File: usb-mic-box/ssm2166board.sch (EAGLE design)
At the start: 10 parts, among them IC1 SSM2166S

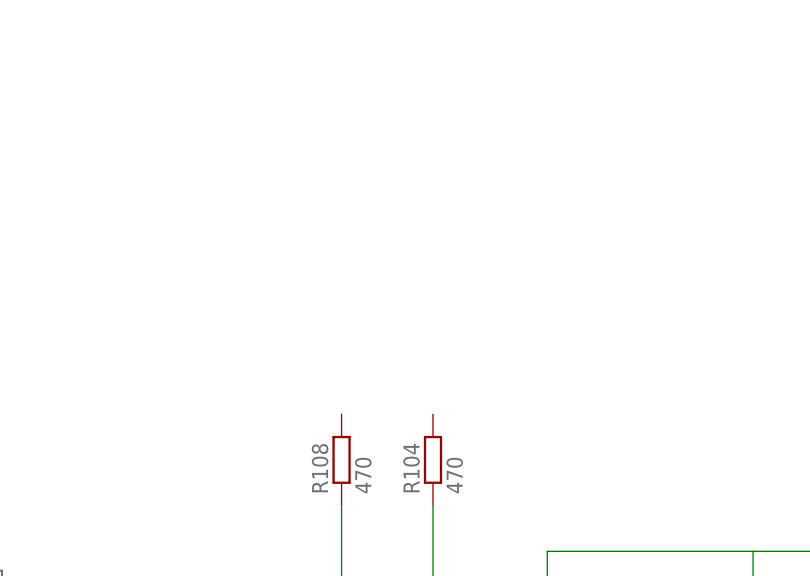
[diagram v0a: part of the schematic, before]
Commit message: Added my first library, and continuing SSM2166 schematics
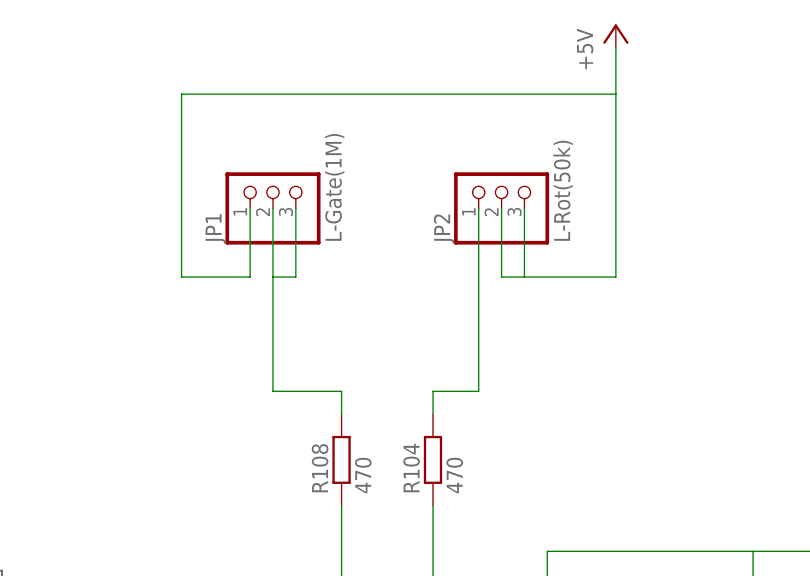
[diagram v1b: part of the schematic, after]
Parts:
- added JP1: L-Gate(1M), anton:PINHD-1X3
- added JP2: L-Rot(50k), anton:PINHD-1X3
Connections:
- new net N$8: JP1.2, JP1.3, R108.2
- new net N$9: JP2.1, R104.2
- net +5V: now also JP1.1, JP2.2, JP2.3
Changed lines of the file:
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@@
 <?xml version="1.0" encoding="utf-8"?>
 <!DOCTYPE eagle SYSTEM "eagle.dtd">
-<eagle version="6.2">
+<eagle version="6.3">
 <drawing>
 <settings>
@@
 <part name="C106" library="rcl" deviceset="CPOL-EU" device="E2-5" value="10uF"/>
 <part name="R181" library="rcl" deviceset="R-EU_" device="R1206" value="4.7k"/>
+<part name="JP1" library="anton" deviceset="PINHD-1X3" device="" value="L-Gate(1M)"/>
+<part name="JP2" library="anton" deviceset="PINHD-1X3" device="" value="L-Rot(50k)"/>
+<part name="P+2" library="supply1" deviceset="+5V" device=""/>
 </parts>
 <sheets>
@@
 <instance part="C106" gate="G$1" x="116.84" y="101.6" rot="R90"/>
 <instance part="R181" gate="G$1" x="139.7" y="111.76"/>
+<instance part="JP1" gate="A" x="73.66" y="152.4" rot="R90"/>
+<instance part="JP2" gate="A" x="99.06" y="152.4" rot="R90"/>
+<instance part="P+2" gate="1" x="111.76" y="170.18"/>
 </instances>
 <busses>
@@
 <pinref part="C103" gate="G$1" pin="1"/>
 <wire x1="15.24" y1="101.6" x2="15.24" y2="104.14" width="0.1524" layer="91"/>
+</segment>
+<segment>
+<pinref part="JP2" gate="A" pin="2"/>
+<wire x1="99.06" y1="149.86" x2="99.06" y2="142.24" width="0.1524" layer="91"/>
+<wire x1="99.06" y1="142.24" x2="101.6" y2="142.24" width="0.1524" layer="91"/>
+<pinref part="JP2" gate="A" pin="3"/>
+<wire x1="101.6" y1="149.86" x2="101.6" y2="142.24" width="0.1524" layer="91"/>
+<wire x1="101.6" y1="142.24" x2="111.76" y2="142.24" width="0.1524" layer="91"/>
+<wire x1="111.76" y1="142.24" x2="111.76" y2="162.56" width="0.1524" layer="91"/>
+<pinref part="P+2" gate="1" pin="+5V"/>
+<wire x1="111.76" y1="162.56" x2="111.76" y2="167.64" width="0.1524" layer="91"/>
+<wire x1="111.76" y1="162.56" x2="63.5" y2="162.56" width="0.1524" layer="91"/>
+<wire x1="63.5" y1="162.56" x2="63.5" y2="142.24" width="0.1524" layer="91"/>
+<wire x1="63.5" y1="142.24" x2="71.12" y2="142.24" width="0.1524" layer="91"/>
+<pinref part="JP1" gate="A" pin="1"/>
+<wire x1="71.12" y1="142.24" x2="71.12" y2="149.86" width="0.1524" layer="91"/>
 </segment>
 </net>
@@
 </segment>
 </net>
+<net name="N$8" class="0">
+<segment>
+<pinref part="R108" gate="G$1" pin="2"/>
+<wire x1="81.28" y1="127" x2="81.28" y2="129.54" width="0.1524" layer="91"/>
+<pinref part="JP1" gate="A" pin="2"/>
+<wire x1="81.28" y1="129.54" x2="73.66" y2="129.54" width="0.1524" layer="91"/>
+<wire x1="73.66" y1="129.54" x2="73.66" y2="142.24" width="0.1524" layer="91"/>
+<wire x1="73.66" y1="149.86" x2="73.66" y2="142.24" width="0.1524" layer="91"/>
+<pinref part="JP1" gate="A" pin="3"/>
+<wire x1="73.66" y1="142.24" x2="76.2" y2="142.24" width="0.1524" layer="91"/>
+<wire x1="76.2" y1="142.24" x2="76.2" y2="149.86" width="0.1524" layer="91"/>
+</segment>
+</net>
+<net name="N$9" class="0">
+<segment>
+<pinref part="R104" gate="G$1" pin="2"/>
+<wire x1="91.44" y1="127" x2="91.44" y2="129.54" width="0.1524" layer="91"/>
+<pinref part="JP2" gate="A" pin="1"/>
+<wire x1="91.44" y1="129.54" x2="96.52" y2="129.54" width="0.1524" layer="91"/>
+<wire x1="96.52" y1="129.54" x2="96.52" y2="149.86" width="0.1524" layer="91"/>
+</segment>
+</net>

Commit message: Continuing SSM2166 board schematics
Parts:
- added C101: 100nF, rcl:C-EUC1206
- added R1, R101: 10k, pot:TRIM_EU-CA6V
- added X1: PG203J, con-hirschmann:PG203J
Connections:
- new net N$10: IC1.-IN, R101.A
- new net N$11: R101.S, R181.2
- new net N$12: C101.1, R1.S, X1.5
- net +5V: now also R1.E
- net AGND: now also X1.1
- net N$3: now also C101.2
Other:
- moved on the sheet: C103
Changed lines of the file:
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@@
 <part name="JP2" library="anton" deviceset="PINHD-1X3" device="" value="L-Rot(50k)"/>
 <part name="P+2" library="supply1" deviceset="+5V" device=""/>
+<part name="R101" library="pot" deviceset="TRIM_EU-" device="CA6V" value="10k"/>
+<part name="C101" library="rcl" deviceset="C-EU" device="C1206" value="100nF"/>
+<part name="R1" library="pot" deviceset="TRIM_EU-" device="CA6V" value="10k"/>
+<part name="X1" library="con-hirschmann" deviceset="PG203J" device=""/>
 </parts>
 <sheets>
@@
 <instances>
 <instance part="IC1" gate="G$1" x="55.88" y="88.9"/>
-<instance part="P+1" gate="1" x="15.24" y="132.08"/>
-<instance part="C103" gate="G$1" x="15.24" y="99.06"/>
-<instance part="SUPPLY1" gate="G$1" x="15.24" y="40.64"/>
+<instance part="P+1" gate="1" x="10.16" y="139.7"/>
+<instance part="C103" gate="G$1" x="10.16" y="96.52"/>
+<instance part="SUPPLY1" gate="G$1" x="10.16" y="40.64"/>
 <instance part="C105" gate="G$1" x="99.06" y="55.88"/>
 <instance part="SUPPLY2" gate="G$1" x="99.06" y="40.64"/>
@@
 <instance part="JP2" gate="A" x="99.06" y="152.4" rot="R90"/>
 <instance part="P+2" gate="1" x="111.76" y="170.18"/>
+<instance part="R101" gate="1" x="152.4" y="111.76" rot="R180"/>
+<instance part="C101" gate="G$1" x="-7.62" y="96.52"/>
+<instance part="R1" gate="1" x="-7.62" y="109.22" rot="R270"/>
+<instance part="X1" gate="1" x="-48.26" y="58.42" rot="R180"/>
 </instances>
 <busses>
@@
 <segment>
 <pinref part="P+1" gate="1" pin="+5V"/>
-<wire x1="15.24" y1="129.54" x2="15.24" y2="104.14" width="0.1524" layer="91"/>
+<wire x1="10.16" y1="137.16" x2="10.16" y2="109.22" width="0.1524" layer="91"/>
 <pinref part="IC1" gate="G$1" pin="V+"/>
-<wire x1="15.24" y1="104.14" x2="38.1" y2="104.14" width="0.1524" layer="91"/>
 <pinref part="C103" gate="G$1" pin="1"/>
-<wire x1="15.24" y1="101.6" x2="15.24" y2="104.14" width="0.1524" layer="91"/>
+<wire x1="10.16" y1="109.22" x2="10.16" y2="104.14" width="0.1524" layer="91"/>
+<wire x1="10.16" y1="104.14" x2="38.1" y2="104.14" width="0.1524" layer="91"/>
+<wire x1="10.16" y1="99.06" x2="10.16" y2="104.14" width="0.1524" layer="91"/>
+<pinref part="R1" gate="1" pin="E"/>
+<wire x1="-2.54" y1="109.22" x2="10.16" y2="109.22" width="0.1524" layer="91"/>
+<junction x="10.16" y="109.22"/>
+<junction x="10.16" y="104.14"/>
 </segment>
 <segment>
@@
 <pinref part="JP1" gate="A" pin="1"/>
 <wire x1="71.12" y1="142.24" x2="71.12" y2="149.86" width="0.1524" layer="91"/>
+<junction x="101.6" y="142.24"/>
+<junction x="111.76" y="162.56"/>
 </segment>
 </net>
@@
 <pinref part="SUPPLY1" gate="G$1" pin="AGND"/>
 <pinref part="C103" gate="G$1" pin="2"/>
-<wire x1="15.24" y1="43.18" x2="15.24" y2="50.8" width="0.1524" layer="91"/>
+<wire x1="10.16" y1="43.18" x2="10.16" y2="50.8" width="0.1524" layer="91"/>
 <pinref part="C190" gate="G$1" pin="2"/>
-<wire x1="15.24" y1="50.8" x2="15.24" y2="93.98" width="0.1524" layer="91"/>
+<wire x1="10.16" y1="50.8" x2="10.16" y2="66.04" width="0.1524" layer="91"/>
+<wire x1="10.16" y1="66.04" x2="10.16" y2="91.44" width="0.1524" layer="91"/>
 <wire x1="22.86" y1="55.88" x2="22.86" y2="50.8" width="0.1524" layer="91"/>
-<wire x1="22.86" y1="50.8" x2="15.24" y2="50.8" width="0.1524" layer="91"/>
+<wire x1="22.86" y1="50.8" x2="10.16" y2="50.8" width="0.1524" layer="91"/>
 <pinref part="IC1" gate="G$1" pin="POWER_DOWN"/>
 <wire x1="38.1" y1="76.2" x2="33.02" y2="76.2" width="0.1524" layer="91"/>
@@
 <pinref part="IC1" gate="G$1" pin="GND"/>
 <wire x1="38.1" y1="73.66" x2="33.02" y2="73.66" width="0.1524" layer="91"/>
+<junction x="33.02" y="73.66"/>
+<junction x="22.86" y="50.8"/>
+<junction x="10.16" y="50.8"/>
+<pinref part="X1" gate="1" pin="1"/>
+<wire x1="-35.56" y1="66.04" x2="10.16" y2="66.04" width="0.1524" layer="91"/>
 </segment>
 <segment>
@@
 <wire x1="111.76" y1="50.8" x2="111.76" y2="48.26" width="0.1524" layer="91"/>
 <wire x1="111.76" y1="48.26" x2="99.06" y2="48.26" width="0.1524" layer="91"/>
+<junction x="99.06" y="48.26"/>
 </segment>
 </net>
@@
 <wire x1="99.06" y1="93.98" x2="129.54" y2="93.98" width="0.1524" layer="91"/>
 <wire x1="129.54" y1="93.98" x2="129.54" y2="78.74" width="0.1524" layer="91"/>
+<junction x="99.06" y="93.98"/>
 </segment>
 </net>
@@
 <wire x1="76.2" y1="96.52" x2="111.76" y2="96.52" width="0.1524" layer="91"/>
 <wire x1="111.76" y1="96.52" x2="111.76" y2="58.42" width="0.1524" layer="91"/>
-</segment>
-</net>
-<net name="N$3" class="0">
-<segment>
-<pinref part="C190" gate="G$1" pin="1"/>
-<wire x1="22.86" y1="63.5" x2="22.86" y2="86.36" width="0.1524" layer="91"/>
-<pinref part="IC1" gate="G$1" pin="+IN"/>
-<wire x1="22.86" y1="86.36" x2="38.1" y2="86.36" width="0.1524" layer="91"/>
 </segment>
 </net>
@@
 <pinref part="R181" gate="G$1" pin="1"/>
 <wire x1="134.62" y1="111.76" x2="127" y2="111.76" width="0.1524" layer="91"/>
+<junction x="127" y="111.76"/>
 </segment>
 </net>
@@
 <wire x1="73.66" y1="142.24" x2="76.2" y2="142.24" width="0.1524" layer="91"/>
 <wire x1="76.2" y1="142.24" x2="76.2" y2="149.86" width="0.1524" layer="91"/>
+<junction x="73.66" y="142.24"/>
 </segment>
 </net>
@@
 </segment>
 </net>
+<net name="N$10" class="0">
+<segment>
+<pinref part="IC1" gate="G$1" pin="-IN"/>
+<wire x1="38.1" y1="91.44" x2="33.02" y2="91.44" width="0.1524" layer="91"/>
+<wire x1="33.02" y1="91.44" x2="33.02" y2="132.08" width="0.1524" layer="91"/>
+<pinref part="R101" gate="1" pin="A"/>
+<wire x1="33.02" y1="132.08" x2="152.4" y2="132.08" width="0.1524" layer="91"/>
+<wire x1="152.4" y1="132.08" x2="152.4" y2="116.84" width="0.1524" layer="91"/>
+</segment>
+</net>
+<net name="N$11" class="0">
+<segment>
+<pinref part="R101" gate="1" pin="S"/>
+<pinref part="R181" gate="G$1" pin="2"/>
+<wire x1="147.32" y1="111.76" x2="144.78" y2="111.76" width="0.1524" layer="91"/>
+</segment>
+</net>
+<net name="N$3" class="0">
+<segment>
+<pinref part="IC1" gate="G$1" pin="+IN"/>
+<wire x1="22.86" y1="86.36" x2="38.1" y2="86.36" width="0.1524" layer="91"/>
+<pinref part="C190" gate="G$1" pin="1"/>
+<wire x1="22.86" y1="63.5" x2="22.86" y2="86.36" width="0.1524" layer="91"/>
+<wire x1="22.86" y1="86.36" x2="-7.62" y2="86.36" width="0.1524" layer="91"/>
+<pinref part="C101" gate="G$1" pin="2"/>
+<wire x1="-7.62" y1="86.36" x2="-7.62" y2="91.44" width="0.1524" layer="91"/>
+<junction x="22.86" y="86.36"/>
+</segment>
+</net>
+<net name="N$12" class="0">
+<segment>
+<pinref part="C101" gate="G$1" pin="1"/>
+<pinref part="R1" gate="1" pin="S"/>
+<wire x1="-7.62" y1="99.06" x2="-7.62" y2="101.6" width="0.1524" layer="91"/>
+<pinref part="X1" gate="1" pin="5"/>
+<wire x1="-7.62" y1="101.6" x2="-7.62" y2="104.14" width="0.1524" layer="91"/>
+<wire x1="-35.56" y1="55.88" x2="-15.24" y2="55.88" width="0.1524" layer="91"/>
+<wire x1="-15.24" y1="55.88" x2="-15.24" y2="101.6" width="0.1524" layer="91"/>
+<wire x1="-15.24" y1="101.6" x2="-7.62" y2="101.6" width="0.1524" layer="91"/>
+</segment>
+</net>

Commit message: Continuing SSM2166 board schematics...
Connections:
- net +5V: now also R1.S; no longer R1.E
- net N$12: no longer R1.S
- net N$3: now also R1.E
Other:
- note added: "Left In"
- note added: "Mic Z"
- note added: "Neg. Feedback Adj."
- moved on the sheet: C101, C103, C105, C107, C190, R1, R104, R108, R109, X1

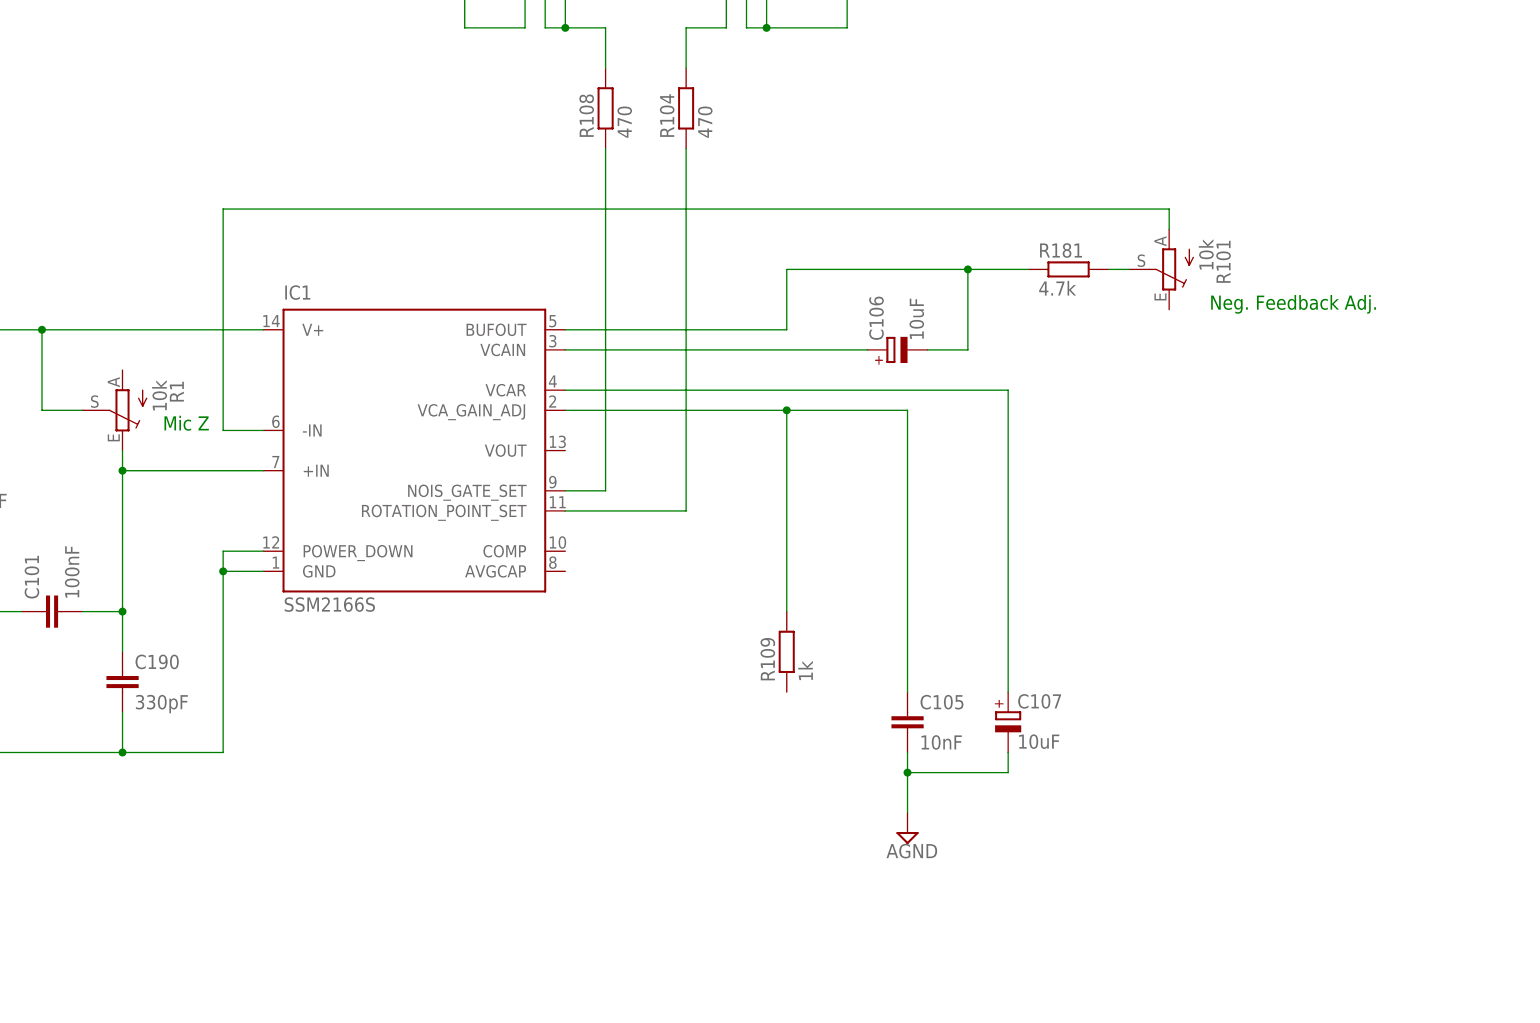
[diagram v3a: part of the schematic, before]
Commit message: Still going on SSM2166 schematics. Just need output and then can clone to Right side?
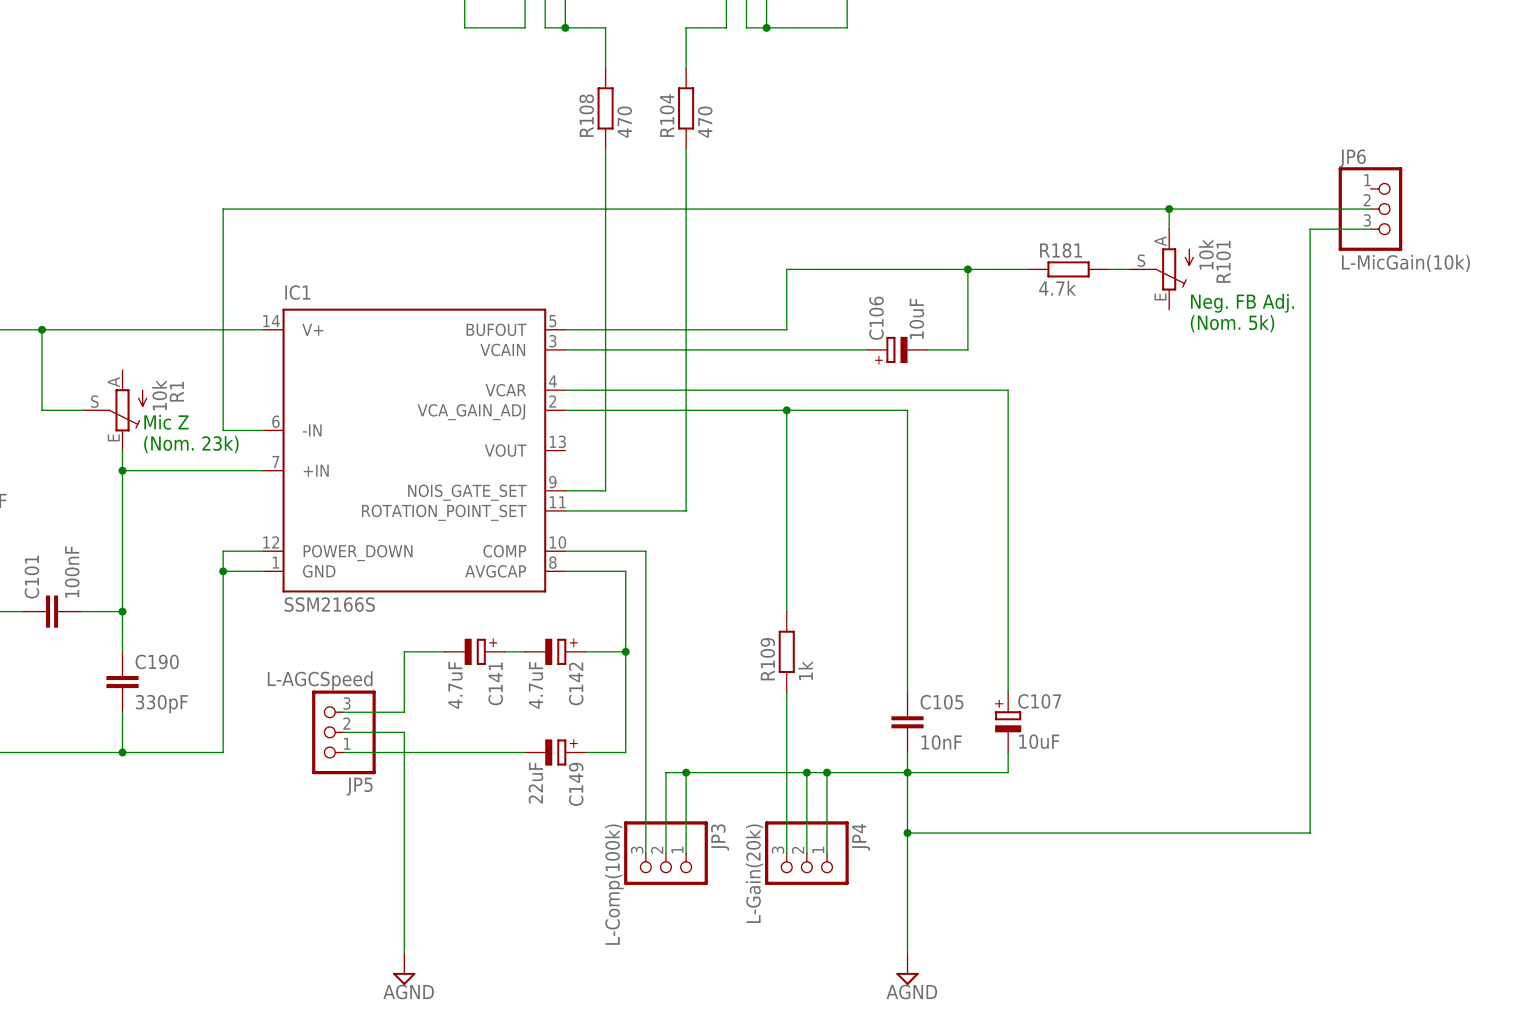
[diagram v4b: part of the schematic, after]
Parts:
- added C141, C142: 4.7uF, resistor:CPOL-EUCT6032
- added C149: 22uF, resistor:CPOL-EUCT7343
- added JP3: L-Comp(100k), anton:PINHD-1X3
- added JP4: L-Gain(20k), anton:PINHD-1X3
- added JP5: L-AGCSpeed, anton:PINHD-1X3
- added JP6: L-MicGain(10k), anton:PINHD-1X3
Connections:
- new net N$14: C141.-, JP5.3
- new net N$15: JP4.3, R109.1
- new net N$16: C141.+, C142.-
- new net N$17: C149.-, JP5.1
- new net N$18: C142.+, C149.+, IC1.AVGCAP
- new net N$8: IC1.COMP, JP3.3
- net AGND: now also JP3.1, JP3.2, JP4.1, JP4.2, JP5.2, JP6.3
- net N$10: now also JP6.2
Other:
- note added: "Mic Z (Nom. 23k)"
- note added: "Neg. FB Adj. (Nom. 5k)"
- note removed: "Mic Z"
- note removed: "Neg. Feedback Adj."
